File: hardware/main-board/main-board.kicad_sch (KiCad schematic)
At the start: 87 parts, among them J1 USB_C_Receptacle_USB2.0, J2 DNI, J3 Display Connector, J4 Conn_01x02, SW1 SW_Push, SW2 SW_Push, SW3 SW_Push, SW4 SW_Push, SW5 SW_Detect, SW6 SW_Boot, U1 TSL2591, U2 STM32L072KZT6, U3 AP2502, U4 USBLC6-2SC6, U5 RT9193, U6 AP2502

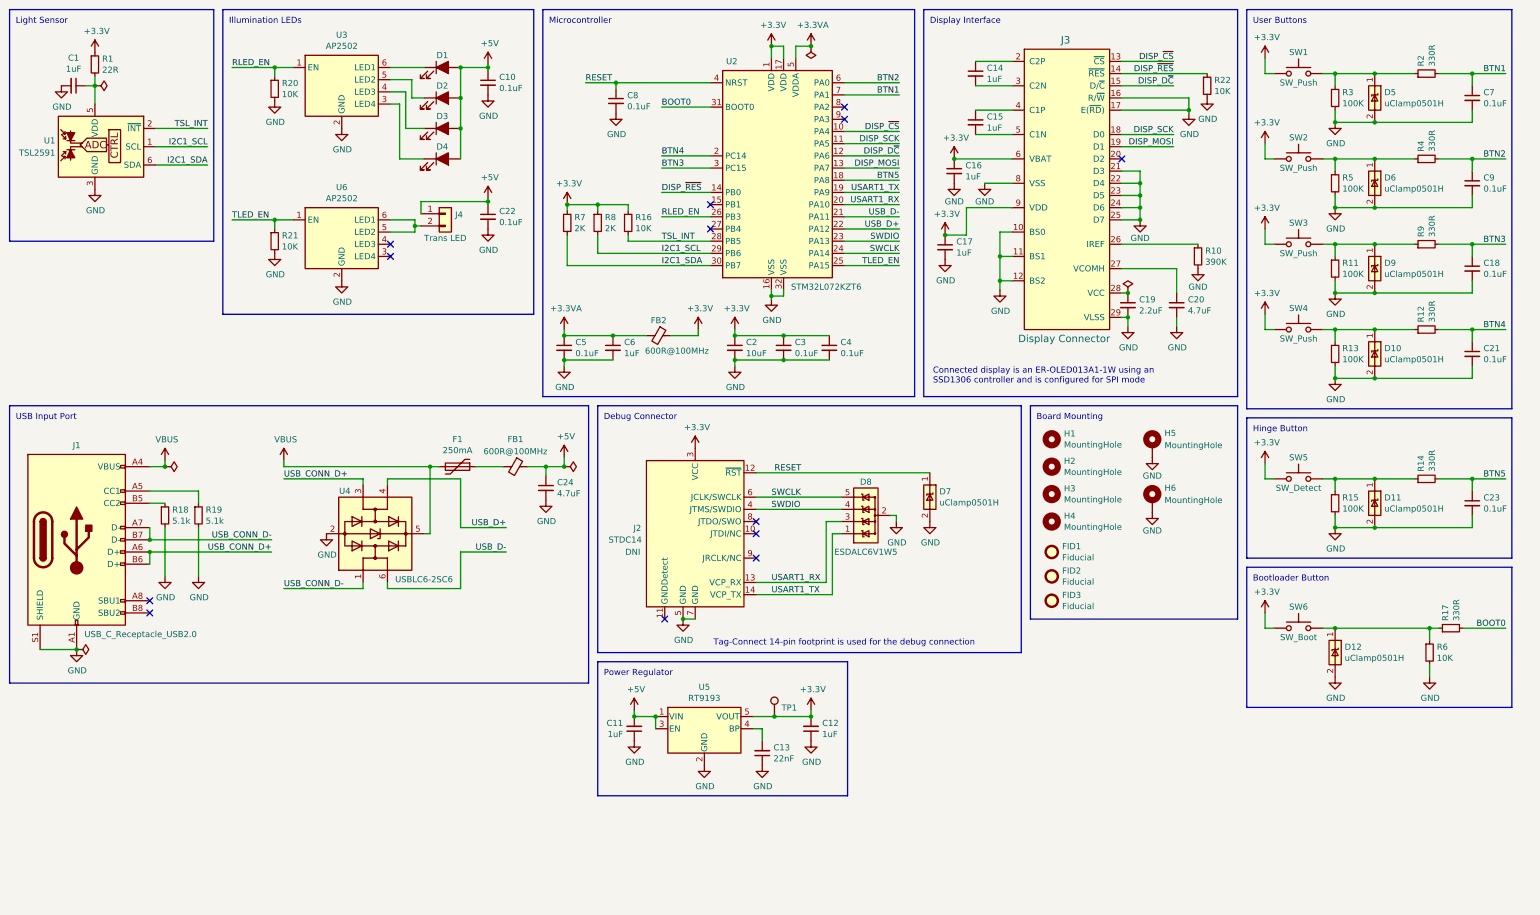
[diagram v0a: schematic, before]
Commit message: Merge hardware from spectrodensitometer project and rename
The spectrodensitometer R&D project is going to be used as the hardware
baseline, rather than the original DPD-100, because it has various
changes that will be useful to this project. Those changes include
different LEDs, different LED drivers, a temperature sensor, and a 1.8V
capable LDO.
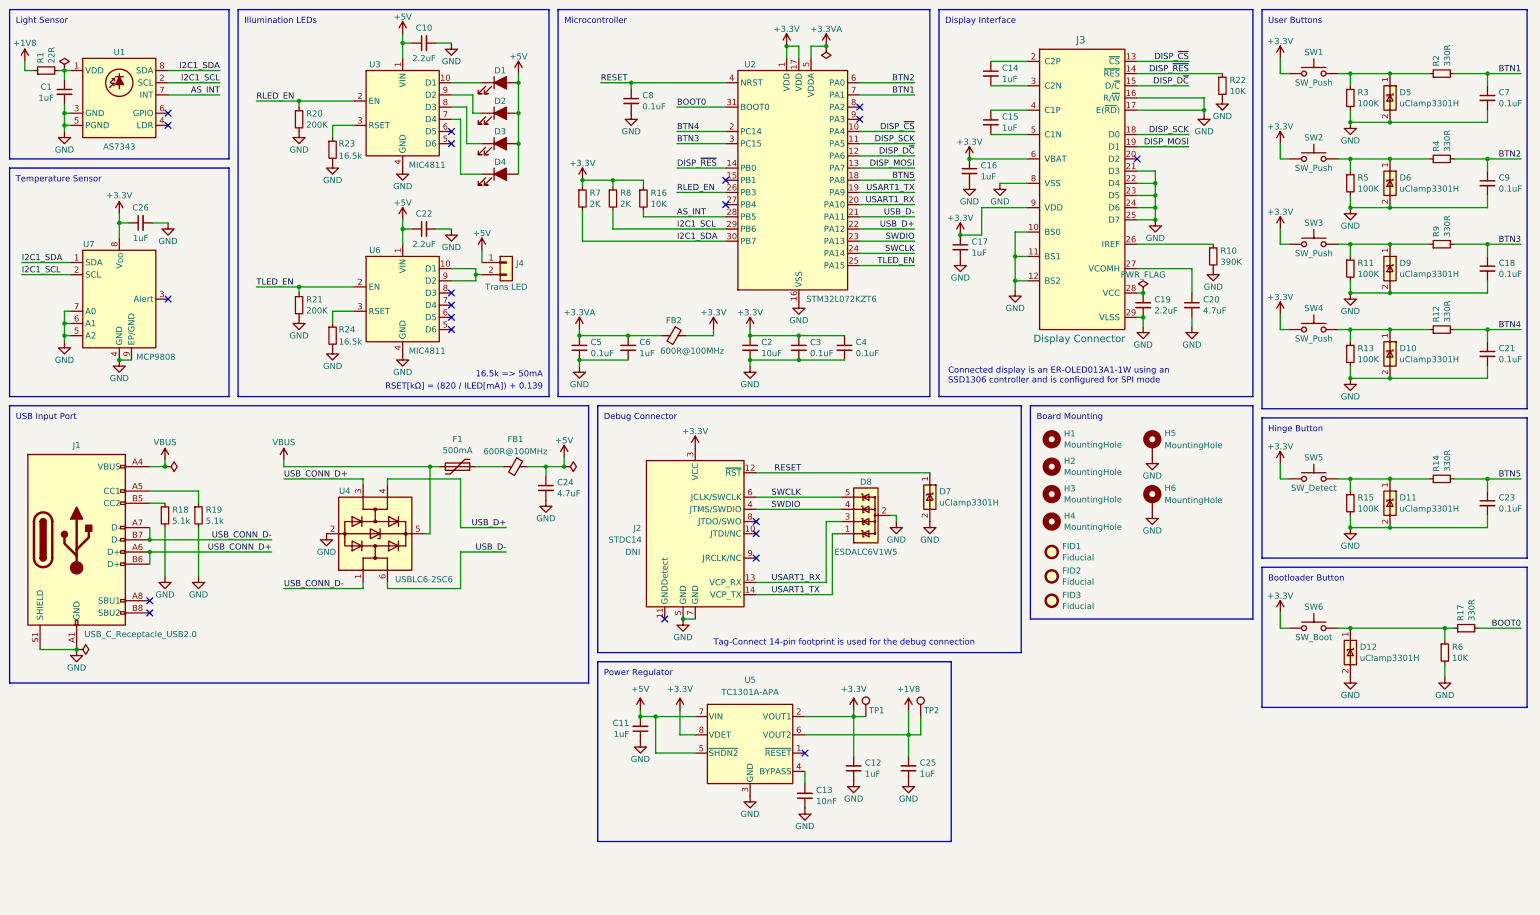
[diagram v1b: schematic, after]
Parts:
- removed U1: TSL2591, lib_fp:AMS_TSL2591, symbol Project:TSL2591
- removed U3, U6: AP2502, Package_TO_SOT_SMD:SOT-23-6, symbol Project:AP2502
- removed U5: RT9193, Package_TO_SOT_SMD:SOT-23-5, symbol Project:RT9193
- added C25: 1uF, Capacitor_SMD:C_0603_1608Metric, symbol Device:C_Small
- added C26: 1uF, Capacitor_SMD:C_0402_1005Metric, symbol Device:C_Small
- added R23, R24: 16.5k, Resistor_SMD:R_0603_1608Metric, symbol Device:R_Small
- added TP2: 1.8V, TestPoint:TestPoint_Pad_D2.0mm, symbol Connector:TestPoint
- added U1: AS7343, lib_fp:AMS_OLGA-8_2.0x3.1mm_P0.8mm, symbol Project:AS7343
- added U3, U6: MIC4811, Package_SO:MSOP-10_3x3mm_P0.5mm, symbol Project:MIC4811
- added U5: TC1301A-APA, Package_SO:MSOP-8_3x3mm_P0.65mm, symbol Project:TC1301A
- added U7: MCP9808, Package_DFN_QFN:DFN-8-1EP_3x2mm_P0.5mm_EP1.7x1.4mm, symbol Sensor_Temperature:MCP9808_DFN
- C10, C22: value 0.1uF -> 2.2uF; Manufacturer PN CL10B104KA8NNNC -> CL10B225KP8NNNC; Supplier PN C1590 -> C100082
- C13: value 22nF -> 10nF; Manufacturer TDK Corporation -> Samsung Electro-Mechanic; Manufacturer PN C2012C0G1H223JT000N -> CL21B103KBANNNC; Supplier LCSC -> Digi-Key; Supplier PN C342593 -> 1276-1015-1-ND
- D1, D2, D3, D4: footprint lib_fp:LED_WL-SWTP-3022-1MP -> lib_fp:SunLike_LED_S1S0; Manufacturer Würth Elektronik -> Seoul Semiconductor Inc.; Manufacturer PN 158302250 -> S1S0-3030659503-0000003S-0P001; Supplier Mouser -> Digi-Key; Supplier PN 710-158302250 -> 897-S1S0-3030659503-0000003S-0P001CT-ND
- D10, D11, D12, D5, D6, D7, D9: value uClamp0501H -> uClamp3301H; Manufacturer PN UCLAMP0501H.TCT -> UCLAMP3301H.TCT; Supplier PN UCLAMP0501HCT-ND -> UCLAMP3301HCT-ND
- F1: value 250mA -> 500mA; Manufacturer PN 1206L025YR -> 1206L050YR; Supplier Mouser -> Digi-Key; Supplier PN 576-1206L025YR -> F2112CT-ND
- FB1, FB2: Manufacturer PN MMZ1608B601CTAH0 -> MMZ1608R601ATD25; Supplier LCSC -> Digi-Key; Supplier PN C97120 -> 445-MMZ1608R601ATD25CT-ND
- R20, R21: value 10K -> 200K; Manufacturer Yaego -> TE Connectivity; Manufacturer PN RC0603JR-0710KL -> CPF0603F200KC1; Supplier LCSC -> Digi-Key; Supplier PN C99198 -> A102235CT-ND
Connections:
- net +3.3V: now also C26.1, U5.2 (VOUT1), U5.8 (VDET), U7.8 (V_{DD}); no longer R1.1
- net +5V: now also U3.1 (VIN), U5.5 (~{SHDN2}), U5.7 (VIN), U6.1 (VIN)
- net GND: now also C25.1, C26.2, R23.2, R24.2, U1.3 (GND), U1.5 (PGND), U3.4 (GND), U5.3 (GND), U6.4 (GND), U7.4 (GND), U7.5 (A2), U7.6 (A1), U7.7 (A0), U7.9 (EP/GND)
- net I2C1_SCL: now also U1.2 (SCL), U7.2 (SCL)
- net I2C1_SDA: now also U1.8 (SDA), U7.1 (SDA)
- net RLED_EN: now also U3.2 (EN)
- net TLED_EN: now also U6.2 (EN)
- net at C13.2: now also U5.4 (BYPASS)
- net at D1.1 (K): now also U3.10 (D1)
- net at C1.1, R1.2: now also U1.1 (VDD)
- net at D2.1 (K): now also U3.9 (D2)
- net at D3.1 (K): now also U3.8 (D3)
- net at D4.1 (K): now also U3.7 (D4)
- net at J4.2 (Pin_2): now also U6.10 (D1), U6.9 (D2)
- net TSL_INT renamed AS_INT
- net AS_INT: now also U1.7 (INT)
- new net: R24.1, U6.3 (RSET)
- new net: R23.1, U3.3 (RSET)
- new net +1V8: C25.2, R1.1, TP2.1, U5.6 (VOUT2)
- no-connect marks 13 -> 21
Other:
- note added: "16.5k => 50mA"
- note added: "RSET[kΩ] = (820 / ILED[mA]) + 0.139"
- note added: "Temperature Sensor"
- title: Printalyzer Densitometer - Main Board -> Printalyzer UV/VIS Densitometer - Main Board
- moved on the sheet: C1, C11, C12, C13, C14, C15, C16, C17, C18, C19, C2, C20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

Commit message: Update schematic for UV/VIS requirements
Switch the light sensor to the TSL2585
Change the reflection LEDs to the 3000K version
Add an additional LED driver for the transmission board
Fix the TVS diodes
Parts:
- removed C1: 1uF, Capacitor_SMD:C_0402_1005Metric, symbol Device:C_Small
- removed J4: Conn_01x02, Connector_JST:JST_SH_BM02B-SRSS-TB_1x02-1MP_P1.00mm_Vertical, symbol Connector_Generic:Conn_01x02
- removed U1: AS7343, lib_fp:AMS_OLGA-8_2.0x3.1mm_P0.8mm, symbol Project:AS7343
- added C2: 1uF, Capacitor_SMD:C_0402_1005Metric, symbol Device:C_Small
- added C28: 2.2uF, Capacitor_SMD:C_0603_1608Metric, symbol Device:C_Small
- added C4: 4.7uF, Capacitor_SMD:C_0402_1005Metric, symbol Device:C_Small
- added J4: Conn_01x04, Connector_JST:JST_SH_BM02B-SRSS-TB_1x04-1MP_P1.00mm_Vertical, symbol Connector_Generic:Conn_01x04
- added R25: 200K, Resistor_SMD:R_0603_1608Metric, symbol Device:R_Small
- added R26: 16.5k, Resistor_SMD:R_0603_1608Metric, symbol Device:R_Small
- added U1: TSL2585, lib_fp:AMS_TSL2585_OLGA-6_2x1mm_P0.65mm, symbol Project:TSL2585
- added U8: MIC4811, Package_SO:MSOP-10_3x3mm_P0.5mm, symbol Project:MIC4811
- D1, D2, D3, D4: Manufacturer PN S1S0-3030659503-0000003S-0P001 -> S1S0-3030309503-0000003S-0P001; Supplier PN 897-S1S0-3030659503-0000003S-0P001CT-ND -> 897-S1S0-3030309503-0000003S-0P001CT-ND
- D10, D11, D12, D5, D6, D7, D9: value uClamp3301H -> uClamp0501H; Manufacturer PN UCLAMP3301H.TCT -> UCLAMP0501H.TCT; Supplier PN UCLAMP3301HCT-ND -> UCLAMP0501HCT-ND
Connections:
- net +1V8: now also R1.2, C4.1; no longer R1.1
- net +5V: now also C28.1, J4.1 (Pin_1), U8.1 (VIN)
- net GND: now also C2.2, C28.2, C4.2, R25.2, R26.2, U1.3 (VSS), U8.4 (GND)
- net I2C1_SCL: now also U1.4 (SCL)
- net I2C1_SDA: now also U1.6 (SDA)
- net at U6.10 (D1), U6.9 (D2): now also J4.2 (Pin_2)
- net TULED_EN: now reaches U2.8 (PA2)
- net TULED_EN: now also R25.1, U8.2 (EN)
- net AS_INT renamed TSL_INT
- net TSL_INT: now also U1.5 (INT)
- net TLED_EN renamed TVLED_EN
- new net: C2.1, R1.1, U1.1 (VDD)
- new net: J4.3 (Pin_3), U8.10 (D1), U8.9 (D2)
- new net: R26.1, U8.3 (RSET)
- new net: J4.4 (Pin_4), U8.7 (D4), U8.8 (D3)
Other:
- note added: "TULED_EN may need a 10K pull-down to overpower the MCU pull-up when in bootloader mode."
- moved on the sheet: C24, C26, F1, FB1, J1, R18, R19, U4, U7

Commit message: Fix misnamed footprint
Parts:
- J4: footprint Connector_JST:JST_SH_BM02B-SRSS-TB_1x04-1MP_P1.00mm_Vertical -> Connector_JST:JST_SH_BM04B-SRSS-TB_1x04-1MP_P1.00mm_Vertical
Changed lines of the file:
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@@
       (effects (font (size 1.27 1.27)) (justify left) hide)
     )
-    (property "Footprint" "Connector_JST:JST_SH_BM02B-SRSS-TB_1x04-1MP_P1.00mm_Vertical" (at 120.65 69.85 0)
+    (property "Footprint" "Connector_JST:JST_SH_BM04B-SRSS-TB_1x04-1MP_P1.00mm_Vertical" (at 120.65 69.85 0)
       (effects (font (size 1.27 1.27)) hide)
     )
